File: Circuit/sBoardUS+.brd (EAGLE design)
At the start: 50 x 50 mm, 37 parts, among them IC4 MC1525TT

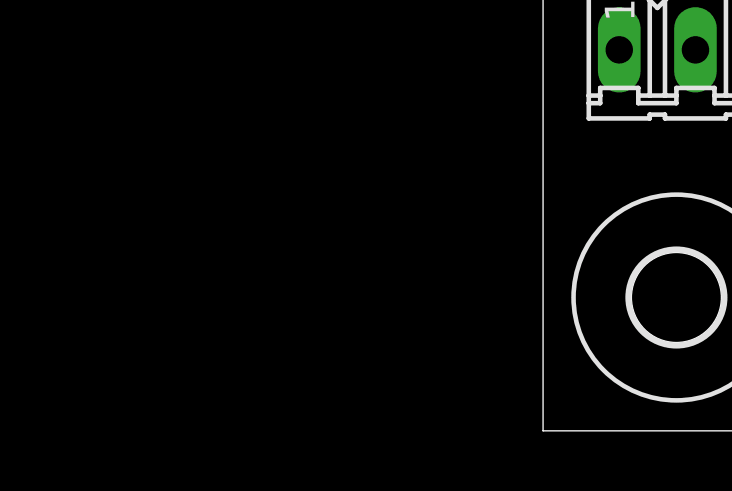
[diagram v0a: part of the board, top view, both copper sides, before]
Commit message: Aggiunti i pad per la programmazione ICSP
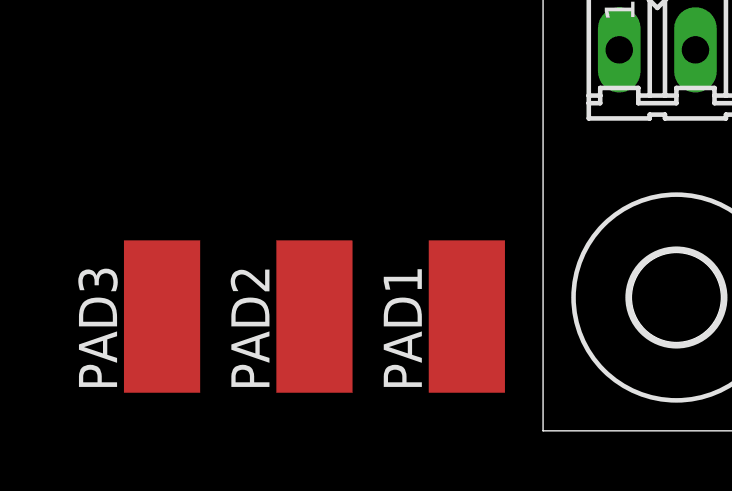
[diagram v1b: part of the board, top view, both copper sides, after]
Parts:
- added PAD1: MCLR, wirepad:SMD2,54-5,08
- added PAD2: PGD, wirepad:SMD2,54-5,08
- added PAD3: PGC, wirepad:SMD2,54-5,08
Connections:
- net N$10: now also PAD2.1
- net N$4: now also PAD1.1
- net N$9: now also PAD3.1
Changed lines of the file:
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@@
 <element name="C6" library="rcl" package="C0805" value="" x="33.02" y="15.24" rot="R90"/>
 <element name="C7" library="rcl" package="C0805" value="" x="35.56" y="15.24" rot="R90"/>
+<element name="PAD1" library="wirepad" package="SMD2,54-5,08" value="MCLR" x="-2.54" y="3.81"/>
+<element name="PAD2" library="wirepad" package="SMD2,54-5,08" value="PGD" x="-7.62" y="3.81"/>
+<element name="PAD3" library="wirepad" package="SMD2,54-5,08" value="PGC" x="-12.7" y="3.81"/>
 </elements>
 <signals>
@@
 </signal>
 <signal name="VCC">
-<contactref element="R1" pad="2"/>
 <contactref element="SL12" pad="3"/>
 <contactref element="SL13" pad="3"/>
@@
 <contactref element="IC4" pad="2"/>
 <contactref element="C7" pad="1"/>
+<contactref element="R1" pad="2"/>
 <wire x1="40.64" y1="35.56" x2="36.83" y2="45.72" width="0" layer="19" extent="1-1"/>
 <wire x1="34.29" y1="32.7" x2="40.64" y2="35.56" width="0" layer="19" extent="1-1"/>
@@
 <wire x1="40.64" y1="12.7" x2="40.64" y2="20.32" width="0" layer="19" extent="1-1"/>
 <wire x1="35.56" y1="14.29" x2="40.64" y2="12.7" width="0" layer="19" extent="1-1"/>
-<wire x1="33.34" y1="9.06" x2="35.56" y2="14.29" width="0" layer="19" extent="1-1"/>
+<wire x1="33.34" y1="9.06" x2="35.56" y2="14.29" width="0" layer="19" extent="1-16"/>
+<wire x1="26.35" y1="8.89" x2="33.34" y2="9.06" width="0" layer="19" extent="1-16"/>
+<wire x1="20.32" y1="8.57" x2="26.35" y2="8.89" width="0" layer="19" extent="1-16"/>
+<wire x1="18.415" y1="11.9634" x2="20.32" y2="8.57" width="0" layer="19" extent="16-16"/>
 <wire x1="28.4734" y1="19.05" x2="35.56" y2="14.29" width="0" layer="19" extent="1-1"/>
-<wire x1="26.35" y1="8.89" x2="33.34" y2="9.06" width="0" layer="19" extent="1-1"/>
-<wire x1="20.32" y1="8.57" x2="26.35" y2="8.89" width="0" layer="19" extent="1-1"/>
-<wire x1="18.415" y1="11.9634" x2="20.32" y2="8.57" width="0" layer="19" extent="1-1"/>
-<wire x1="2.54" y1="12.7" x2="18.415" y2="11.9634" width="0" layer="19" extent="1-1"/>
+<wire x1="2.54" y1="12.7" x2="18.415" y2="11.9634" width="0" layer="19" extent="16-16"/>
 <wire x1="2.54" y1="20.32" x2="2.54" y2="12.7" width="0" layer="19" extent="1-1"/>
 <wire x1="2.54" y1="27.94" x2="2.54" y2="20.32" width="0" layer="19" extent="1-1"/>
@@
 <contactref element="IC2" pad="8"/>
 <contactref element="IC1" pad="27"/>
+<contactref element="PAD3" pad="1"/>
 <wire x1="28.4734" y1="11.43" x2="30.18" y2="38.1" width="0" layer="19" extent="1-1"/>
+<wire x1="-12.7" y1="3.81" x2="28.4734" y2="11.43" width="0" layer="19" extent="1-1"/>
 </signal>
 <signal name="N$10">
 <contactref element="IC1" pad="28"/>
 <contactref element="IC2" pad="11"/>
+<contactref element="PAD2" pad="1"/>
 <wire x1="28.4734" y1="15.24" x2="30.18" y2="39.37" width="0" layer="19" extent="1-1"/>
+<wire x1="-7.62" y1="3.81" x2="28.4734" y2="15.24" width="0" layer="19" extent="1-1"/>
 </signal>
 <signal name="N$12">
@@
 <contactref element="IC1" pad="1"/>
 <contactref element="R1" pad="1"/>
+<contactref element="PAD1" pad="1"/>
 <wire x1="14.29" y1="39.37" x2="20.62" y2="39.37" width="0" layer="19" extent="1-1"/>
+<wire x1="-2.54" y1="3.81" x2="14.29" y2="39.37" width="0" layer="19" extent="1-1"/>
 </signal>
 <signal name="N$29">
